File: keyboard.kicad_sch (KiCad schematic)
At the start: 86 parts, among them J3 Conn_01x12_Pin, SW10 SW_SPST, SW11 SW_SPST, SW12 SW_SPST, SW13 SW_SPST, SW14 SW_SPST, SW15 SW_SPST, SW16 SW_SPST, SW17 SW_SPST, SW18 SW_SPST, SW19 SW_SPST, SW20 SW_SPST, SW21 SW_SPST, SW22 SW_SPST, SW23 SW_SPST, SW24 SW_SPST, SW25 SW_SPST, SW26 SW_SPST, SW27 SW_SPST, SW28 SW_SPST, SW29 SW_SPST, SW3 SW_SPST, SW30 SW_SPST, SW31 SW_SPST, SW32 SW_SPST, SW33 SW_SPST, SW34 SW_SPST, SW35 SW_SPST, SW36 SW_SPST, SW37 SW_SPST, SW38 SW_SPST, SW39 SW_SPST, SW4 SW_SPST, SW5 SW_SPST, SW6 SW_SPST, SW7 SW_SPST, SW8 SW_SPST, SW9 SW_SPST, U17 M110

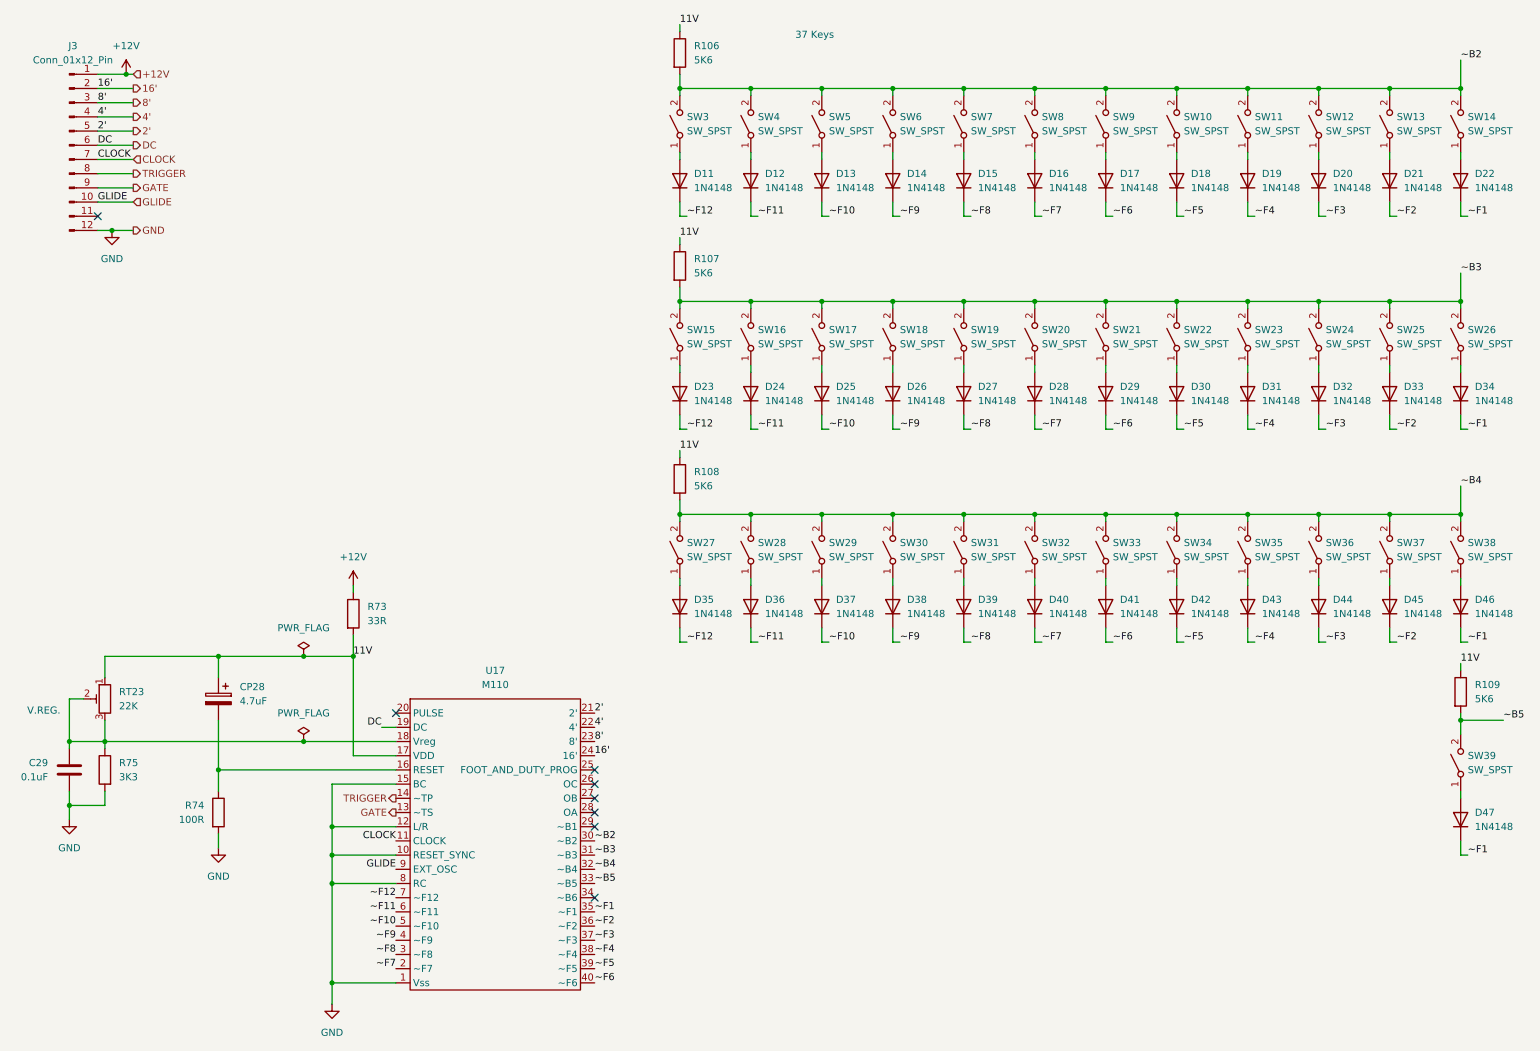
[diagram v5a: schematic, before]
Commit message: Keyboard routing
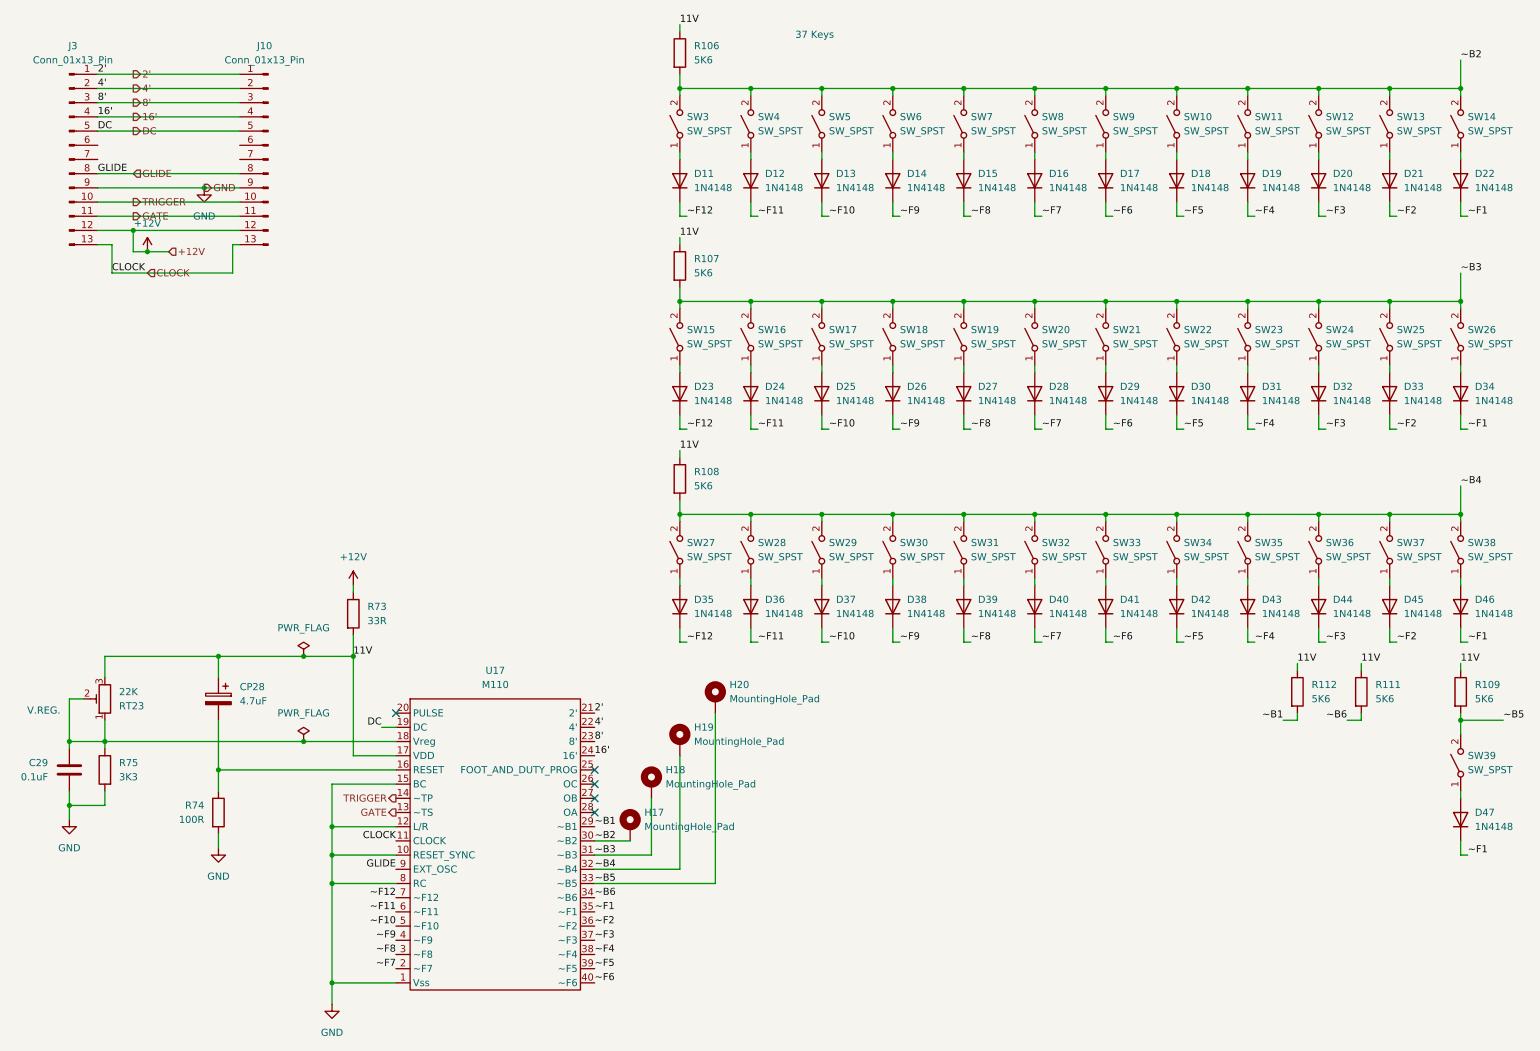
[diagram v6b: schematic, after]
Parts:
- added H17, H18, H19, H20: MountingHole_Pad, MountingHole:MountingHole_2.2mm_M2_Pad, symbol Mechanical:MountingHole_Pad
- added J10: Conn_01x13_Pin, Connector_PinHeader_2.54mm:PinHeader_1x13_P2.54mm_Vertical, symbol Connector:Conn_01x13_Pin
- added R111, R112: 5K6, Resistor_THT:R_Axial_DIN0207_L6.3mm_D2.5mm_P10.16mm_Horizontal, symbol Device:R
- C29: footprint Capacitor_THT:C_Disc_D5.0mm_W2.5mm_P5.00mm -> Capacitor_THT:C_Rect_L11.0mm_W2.8mm_P10.00mm_MKT
- J3: value Conn_01x12_Pin -> Conn_01x13_Pin; footprint Connector_PinHeader_2.54mm:PinHeader_1x12_P2.54mm_Vertical -> Connector_PinHeader_2.54mm:PinHeader_1x13_P2.54mm_Vertical; symbol Connector:Conn_01x12_Pin -> Connector:Conn_01x13_Pin
- R106, R107, R108, R109, R73: footprint Resistor_THT:R_Axial_DIN0204_L3.6mm_D1.6mm_P7.62mm_Horizontal -> Resistor_THT:R_Axial_DIN0207_L6.3mm_D2.5mm_P10.16mm_Horizontal
- R74: footprint Resistor_THT:R_Axial_DIN0204_L3.6mm_D1.6mm_P7.62mm_Horizontal -> Resistor_THT:R_Axial_DIN0207_L6.3mm_D2.5mm_P15.24mm_Horizontal
- R75: footprint Resistor_THT:R_Axial_DIN0204_L3.6mm_D1.6mm_P7.62mm_Horizontal -> Resistor_THT:R_Axial_DIN0309_L9.0mm_D3.2mm_P12.70mm_Horizontal
- RT23: footprint Potentiometer_THT:Potentiometer_Bourns_3339P_Vertical_HandSoldering -> Potentiometer_THT:Potentiometer_Piher_PT-10-V10_Vertical
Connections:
- net +12V: now also J3.12 (Pin_12), J10.12 (Pin_12); no longer J3.1 (Pin_1)
- net 11V: now also RT23.3, R111.1, R112.1; no longer RT23.1
- net 16': now also J3.4 (Pin_4), J10.4 (Pin_4); no longer J3.2 (Pin_2)
- net 2': now also J3.1 (Pin_1), J10.1 (Pin_1); no longer J3.5 (Pin_5)
- net 4': now also J3.2 (Pin_2), J10.2 (Pin_2); no longer J3.4 (Pin_4)
- net 8': now also J10.3 (Pin_3)
- net CLOCK: now also J3.13 (Pin_13), J10.13 (Pin_13); no longer J3.7 (Pin_7)
- net DC: now also J3.5 (Pin_5), J10.5 (Pin_5); no longer J3.6 (Pin_6)
- net GATE: now also J3.11 (Pin_11), J10.11 (Pin_11); no longer J3.9 (Pin_9)
- net GLIDE: now also J3.8 (Pin_8), J10.8 (Pin_8); no longer J3.10 (Pin_10)
- net GND: now also J3.9 (Pin_9), J10.9 (Pin_9); no longer J3.12 (Pin_12)
- net TRIGGER: now also J3.10 (Pin_10), J10.10 (Pin_10); no longer J3.8 (Pin_8)
- net ~B2: now also H17.1
- net ~B3: now also H18.1
- net ~B4: now also H19.1
- net ~B5: now also H20.1
- net at C29.1, R75.1, RT23.2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: now also RT23.1; no longer RT23.3
- net ~B1: now reaches U17.29 (~B1)
- net ~B1: now also R112.2
- net ~B6: now reaches U17.34 (~B6)
- net ~B6: now also R111.2
- no-connect marks 8 -> 5
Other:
- moved on the sheet: RT23

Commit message: Keyboard routing nearly done
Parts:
- D16, D28, D40: footprint Diode_THT:D_DO-35_SOD27_P12.70mm_Horizontal -> PCM_Jumper_AKL:Jumper_P15.24mm_D1.2mm
- D17, D29: footprint Diode_THT:D_DO-35_SOD27_P12.70mm_Horizontal -> PCM_Jumper_AKL:Jumper_P17.78mm_D1.2mm
- D18, D30: footprint Diode_THT:D_DO-35_SOD27_P12.70mm_Horizontal -> PCM_Jumper_AKL:Jumper_P20.32mm_D1.2mm
- D19, D20, D31, D32, D41, D42: footprint Diode_THT:D_DO-35_SOD27_P12.70mm_Horizontal -> PCM_Jumper_AKL:Jumper_P25.40mm_D1.2mm
- D21, D22, D33, D34, D43, D44, D45, D46: footprint Diode_THT:D_DO-35_SOD27_P12.70mm_Horizontal -> PCM_Jumper_AKL:Jumper_P30.48mm_D1.2mm
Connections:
- net ~F1: now also D11.1 (K), D23.1 (K), D35.1 (K); no longer D22.1 (K), D34.1 (K), D46.1 (K)
- net ~F10: now also D20.1 (K), D32.1 (K), D44.1 (K); no longer D13.1 (K), D25.1 (K), D37.1 (K)
- net ~F11: now also D21.1 (K), D33.1 (K), D45.1 (K); no longer D12.1 (K), D24.1 (K), D36.1 (K)
- net ~F12: now also D22.1 (K), D34.1 (K), D46.1 (K); no longer D11.1 (K), D23.1 (K), D35.1 (K)
- net ~F2: now also D12.1 (K), D24.1 (K), D36.1 (K); no longer D21.1 (K), D33.1 (K), D45.1 (K)
- net ~F3: now also D13.1 (K), D25.1 (K), D37.1 (K); no longer D20.1 (K), D32.1 (K), D44.1 (K)
- net ~F4: now also D14.1 (K), D26.1 (K), D38.1 (K); no longer D19.1 (K), D31.1 (K), D43.1 (K)
- net ~F5: now also D15.1 (K), D27.1 (K), D39.1 (K); no longer D18.1 (K), D30.1 (K), D42.1 (K)
- net ~F6: now also D16.1 (K), D28.1 (K), D40.1 (K); no longer D17.1 (K), D29.1 (K), D41.1 (K)
- net ~F7: now also D17.1 (K), D29.1 (K), D41.1 (K); no longer D16.1 (K), D28.1 (K), D40.1 (K)
- net ~F8: now also D18.1 (K), D30.1 (K), D42.1 (K); no longer D15.1 (K), D27.1 (K), D39.1 (K)
- net ~F9: now also D19.1 (K), D31.1 (K), D43.1 (K); no longer D14.1 (K), D26.1 (K), D38.1 (K)
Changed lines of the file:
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@@
 	)
 	(label "~F6"
-		(at 209.55 49.53 0)
+		(at 196.85 49.53 0)
 		(effects
 			(font
@@
 	)
 	(label "~F12"
-		(at 133.35 125.73 0)
+		(at 273.05 125.73 0)
 		(effects
 			(font
@@
 	)
 	(label "~F9"
-		(at 171.45 49.53 0)
+		(at 234.95 49.53 0)
 		(effects
 			(font
@@
 	)
 	(label "~F7"
-		(at 196.85 49.53 0)
+		(at 209.55 49.53 0)
 		(effects
 			(font
@@
 	)
 	(label "~F1"
-		(at 273.05 49.53 0)
+		(at 133.35 49.53 0)
 		(effects
 			(font
@@
 	)
 	(label "~F7"
-		(at 196.85 125.73 0)
+		(at 209.55 125.73 0)
 		(effects
 			(font
@@
 	)
 	(label "~F9"
-		(at 171.45 125.73 0)
+		(at 234.95 125.73 0)
 		(effects
 			(font
@@
 	)
 	(label "~F12"
-		(at 133.35 87.63 0)
+		(at 273.05 87.63 0)
 		(effects
 			(font
@@
 	)
 	(label "~F6"
-		(at 209.55 87.63 0)
+		(at 196.85 87.63 0)
 		(effects
 			(font
@@
 	)
 	(label "~F8"
-		(at 184.15 125.73 0)
+		(at 222.25 125.73 0)
 		(effects
 			(font
@@
 	)
 	(label "~F3"
-		(at 247.65 125.73 0)
+		(at 158.75 125.73 0)
 		(effects
 			(font
@@
 	)
 	(label "~F1"
-		(at 273.05 125.73 0)
+		(at 133.35 125.73 0)
 		(effects
 			(font
@@
 	)
 	(label "~F2"
-		(at 260.35 125.73 0)
+		(at 146.05 125.73 0)
 		(effects
 			(font
@@
 	)
 	(label "~F10"
-		(at 158.75 49.53 0)
+		(at 247.65 49.53 0)
 		(effects
 			(font
@@
 	)
 	(label "~F11"
-		(at 146.05 125.73 0)
+		(at 260.35 125.73 0)
 		(effects
 			(font
@@
 	)
 	(label "~F8"
-		(at 184.15 49.53 0)
+		(at 222.25 49.53 0)
 		(effects
 			(font
@@
 	)
 	(label "~F4"
-		(at 234.95 87.63 0)
+		(at 171.45 87.63 0)
 		(effects
 			(font
@@
 	)
 	(label "~F5"
-		(at 222.25 49.53 0)
+		(at 184.15 49.53 0)
 		(effects
 			(font
@@
 	)
 	(label "~F4"
-		(at 234.95 49.53 0)
+		(at 171.45 49.53 0)
 		(effects
 			(font
@@
 	)
 	(label "~F4"
-		(at 234.95 125.73 0)
+		(at 171.45 125.73 0)
 		(effects
 			(font
@@
 	)
 	(label "~F11"
-		(at 146.05 49.53 0)
+		(at 260.35 49.53 0)
 		(effects
 			(font
@@
 	)
 	(label "~F8"
-		(at 184.15 87.63 0)
+		(at 222.25 87.63 0)
 		(effects
 			(font
@@
 	)
 	(label "~F1"
-		(at 273.05 87.63 0)
+		(at 133.35 87.63 0)
 		(effects
 			(font
@@
 	)
 	(label "~F2"
-		(at 260.35 87.63 0)
+		(at 146.05 87.63 0)
 		(effects
 			(font
@@
 	)
 	(label "~F10"
-		(at 158.75 87.63 0)
+		(at 247.65 87.63 0)
 		(effects
 			(font
@@
 	)
 	(label "~F2"
-		(at 260.35 49.53 0)
+		(at 146.05 49.53 0)
 		(effects
 			(font
@@
 	)
 	(label "~F7"
-		(at 196.85 87.63 0)
+		(at 209.55 87.63 0)
 		(effects
 			(font
@@
 	)
 	(label "~F9"
-		(at 171.45 87.63 0)
+		(at 234.95 87.63 0)
 		(effects
 			(font
@@
 	)
 	(label "~F3"
-		(at 247.65 49.53 0)
+		(at 158.75 49.53 0)
 		(effects
 			(font
@@
 	)
 	(label "~F5"
-		(at 222.25 87.63 0)
+		(at 184.15 87.63 0)
 		(effects
 			(font
@@
 	)
 	(label "~F12"
-		(at 133.35 49.53 0)
+		(at 273.05 49.53 0)
 		(effects
 			(font
@@
 	)
 	(label "~F6"
-		(at 209.55 125.73 0)
+		(at 196.85 125.73 0)
 		(effects
 			(font
@@
 	)
 	(label "~F11"
-		(at 146.05 87.63 0)
+		(at 260.35 87.63 0)
 		(effects
 			(font
@@
 	)
 	(label "~F10"
-		(at 158.75 125.73 0)
+		(at 247.65 125.73 0)
 		(effects
 			(font
@@
 	)
 	(label "~F3"
-		(at 247.65 87.63 0)
+		(at 158.75 87.63 0)
 		(effects
 			(font
@@
 	)
 	(label "~F5"
-		(at 222.25 125.73 0)
+		(at 184.15 125.73 0)
 		(effects
 			(font
@@
 			)
 		)
-		(property "Footprint" "Diode_THT:D_DO-35_SOD27_P12.70mm_Horizontal"
+		(property "Footprint" "PCM_Jumper_AKL:Jumper_P17.78mm_D1.2mm"
 			(at 208.28 81.28 0)
 			(effects
@@
 			)
 		)
-		(property "Footprint" "Diode_THT:D_DO-35_SOD27_P12.70mm_Horizontal"
+		(property "Footprint" "PCM_Jumper_AKL:Jumper_P25.40mm_D1.2mm"
 			(at 233.68 81.28 0)
 			(effects
@@
 			)
 		)
-		(property "Footprint" "Diode_THT:D_DO-35_SOD27_P12.70mm_Horizontal"
+		(property "Footprint" "PCM_Jumper_AKL:Jumper_P20.32mm_D1.2mm"
 			(at 220.98 43.18 0)
 			(effects
@@
 			)
 		)
-		(property "Footprint" "Diode_THT:D_DO-35_SOD27_P12.70mm_Horizontal"
+		(property "Footprint" "PCM_Jumper_AKL:Jumper_P30.48mm_D1.2mm"
 			(at 246.38 119.38 0)
 			(effects
@@
 			)
 		)
-		(property "Footprint" "Diode_THT:D_DO-35_SOD27_P12.70mm_Horizontal"
+		(property "Footprint" "PCM_Jumper_AKL:Jumper_P25.40mm_D1.2mm"
 			(at 246.38 81.28 0)
 			(effects
@@
 			)
 		)
-		(property "Footprint" "Diode_THT:D_DO-35_SOD27_P12.70mm_Horizontal"
+		(property "Footprint" "PCM_Jumper_AKL:Jumper_P15.24mm_D1.2mm"
 			(at 195.58 119.38 0)
 			(effects
@@
 			)
 		)
-		(property "Footprint" "Diode_THT:D_DO-35_SOD27_P12.70mm_Horizontal"
+		(property "Footprint" "PCM_Jumper_AKL:Jumper_P30.48mm_D1.2mm"
 			(at 271.78 43.18 0)
 			(effects
@@
 			)
 		)
-		(property "Footprint" "Diode_THT:D_DO-35_SOD27_P12.70mm_Horizontal"
+		(property "Footprint" "PCM_Jumper_AKL:Jumper_P25.40mm_D1.2mm"
 			(at 233.68 43.18 0)
 			(effects
@@
 			)
 		)
-		(property "Footprint" "Diode_THT:D_DO-35_SOD27_P12.70mm_Horizontal"
+		(property "Footprint" "PCM_Jumper_AKL:Jumper_P20.32mm_D1.2mm"
 			(at 220.98 81.28 0)
 			(effects
@@
 			)
 		)
-		(property "Footprint" "Diode_THT:D_DO-35_SOD27_P12.70mm_Horizontal"
+		(property "Footprint" "PCM_Jumper_AKL:Jumper_P30.48mm_D1.2mm"
 			(at 259.08 119.38 0)
 			(effects
@@
 			)
 		)
-		(property "Footprint" "Diode_THT:D_DO-35_SOD27_P12.70mm_Horizontal"
+		(property "Footprint" "PCM_Jumper_AKL:Jumper_P25.40mm_D1.2mm"
 			(at 208.28 119.38 0)
 			(effects
@@
 			)
 		)
-		(property "Footprint" "Diode_THT:D_DO-35_SOD27_P12.70mm_Horizontal"
+		(property "Footprint" "PCM_Jumper_AKL:Jumper_P30.48mm_D1.2mm"
 			(at 259.08 43.18 0)
 			(effects
@@
 			)
 		)
-		(property "Footprint" "Diode_THT:D_DO-35_SOD27_P12.70mm_Horizontal"
+		(property "Footprint" "PCM_Jumper_AKL:Jumper_P17.78mm_D1.2mm"
 			(at 208.28 43.18 0)
 			(effects
@@
 			)
 		)
-		(property "Footprint" "Diode_THT:D_DO-35_SOD27_P12.70mm_Horizontal"
+		(property "Footprint" "PCM_Jumper_AKL:Jumper_P15.24mm_D1.2mm"
 			(at 195.58 81.28 0)
 			(effects
@@
 			)
 		)
-		(property "Footprint" "Diode_THT:D_DO-35_SOD27_P12.70mm_Horizontal"
+		(property "Footprint" "PCM_Jumper_AKL:Jumper_P30.48mm_D1.2mm"
 			(at 271.78 119.38 0)
 			(effects
@@
 			)
 		)
-		(property "Footprint" "Diode_THT:D_DO-35_SOD27_P12.70mm_Horizontal"
+		(property "Footprint" "PCM_Jumper_AKL:Jumper_P25.40mm_D1.2mm"
 			(at 220.98 119.38 0)
 			(effects
@@
 			)
 		)
-		(property "Footprint" "Diode_THT:D_DO-35_SOD27_P12.70mm_Horizontal"
+		(property "Footprint" "PCM_Jumper_AKL:Jumper_P30.48mm_D1.2mm"
 			(at 259.08 81.28 0)
 			(effects
@@
 			)
 		)
-		(property "Footprint" "Diode_THT:D_DO-35_SOD27_P12.70mm_Horizontal"
+		(property "Footprint" "PCM_Jumper_AKL:Jumper_P30.48mm_D1.2mm"
 			(at 233.68 119.38 0)
 			(effects
@@
 			)
 		)
-		(property "Footprint" "Diode_THT:D_DO-35_SOD27_P12.70mm_Horizontal"
+		(property "Footprint" "PCM_Jumper_AKL:Jumper_P25.40mm_D1.2mm"
 			(at 246.38 43.18 0)
 			(effects
@@
 			)
 		)
-		(property "Footprint" "Diode_THT:D_DO-35_SOD27_P12.70mm_Horizontal"
+		(property "Footprint" "PCM_Jumper_AKL:Jumper_P30.48mm_D1.2mm"
 			(at 271.78 81.28 0)
 			(effects
@@
 			)
 		)
-		(property "Footprint" "Diode_THT:D_DO-35_SOD27_P12.70mm_Horizontal"
+		(property "Footprint" "PCM_Jumper_AKL:Jumper_P15.24mm_D1.2mm"
 			(at 195.58 43.18 0)
 			(effects
